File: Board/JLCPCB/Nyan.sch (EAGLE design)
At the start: 63 parts, among them IC1 74HCT541PW, IC2 STM32F10XCXT6, IC3 74HCT541PW, IC4 ST3485, U2 A4988_STEP, U3 MAX6966, X1 WR-WTB2.0-2_THT-VER, X10 32768, X2 WR-WTB2.0-4_THT_VER, X3 WR-WTB2.0-5_THT-VER, X4 WR-WTB2.0-5_THT-VER, X6 68610614122, X7 68612414422, X8 68610414122, X9 8M

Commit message: [Board] A little more layouting done
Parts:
- removed SV1: (no value), con-lstb:MA03-2
- added JP1, JP2: (no value), jumper:JP1E
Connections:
- removed net N$12: R6.2, SV1.2
- removed net N$13: R7.2, SV1.1
- net +3V3: now also JP1.2, JP2.2; no longer SV1.5, SV1.6
- net BOOT1: now also JP2.1, R6.2; no longer SV1.4
- net N$7: now also JP1.1, R7.2; no longer SV1.3
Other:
- moved on the sheet: R6, R7
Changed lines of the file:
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@@
 <part name="SJ1" library="jumper" deviceset="SJ2W" device=""/>
 <part name="SJ2" library="jumper" deviceset="SJ2W" device=""/>
-<part name="SV1" library="con-lstb" deviceset="MA03-2" device=""/>
 <part name="+3V6" library="supply1" deviceset="+3V3" device=""/>
 <part name="R6" library="rcl" deviceset="R-EU_" device="R0603" value="10k"/>
@@
 <part name="C21" library="rcl" deviceset="C-EU" device="C0603" value="1u"/>
 <part name="X3" library="TURAG_Steckverbinder" deviceset="WR-WTB2.0-5" device="_THT-VER"/>
+<part name="JP1" library="jumper" deviceset="JP1E" device=""/>
+<part name="JP2" library="jumper" deviceset="JP1E" device=""/>
 </parts>
 <sheets>
@@
 <instance part="SJ1" gate="G$1" x="40.64" y="30.48" rot="R90"/>
 <instance part="SJ2" gate="G$1" x="40.64" y="12.7" rot="R270"/>
-<instance part="SV1" gate="1" x="27.94" y="-88.9"/>
-<instance part="+3V6" gate="G$1" x="43.18" y="-73.66"/>
-<instance part="R6" gate="G$1" x="17.78" y="-99.06" rot="MR90"/>
-<instance part="R7" gate="G$1" x="38.1" y="-99.06" rot="MR90"/>
+<instance part="+3V6" gate="G$1" x="27.94" y="-73.66"/>
+<instance part="R6" gate="G$1" x="12.7" y="-96.52" rot="MR90"/>
+<instance part="R7" gate="G$1" x="43.18" y="-96.52" rot="MR90"/>
 <instance part="GND15" gate="1" x="58.42" y="-58.42" rot="MR0"/>
 <instance part="GND16" gate="1" x="27.94" y="-111.76" rot="MR0"/>
@@
 <instance part="C21" gate="G$1" x="27.94" y="-43.18" rot="MR180"/>
 <instance part="X3" gate="G$1" x="33.02" y="73.66" rot="R180"/>
+<instance part="JP1" gate="A" x="33.02" y="-88.9" rot="R90"/>
+<instance part="JP2" gate="A" x="22.86" y="-88.9" rot="MR90"/>
 </instances>
 <busses>
@@
 <segment>
 <pinref part="R6" gate="G$1" pin="1"/>
-<wire x1="17.78" y1="-104.14" x2="17.78" y2="-106.68" width="0.1524" layer="91"/>
-<wire x1="17.78" y1="-106.68" x2="27.94" y2="-106.68" width="0.1524" layer="91"/>
+<wire x1="12.7" y1="-101.6" x2="12.7" y2="-106.68" width="0.1524" layer="91"/>
 <pinref part="GND16" gate="1" pin="GND"/>
+<wire x1="12.7" y1="-106.68" x2="27.94" y2="-106.68" width="0.1524" layer="91"/>
 <wire x1="27.94" y1="-106.68" x2="27.94" y2="-109.22" width="0.1524" layer="91"/>
 <pinref part="R7" gate="G$1" pin="1"/>
-<wire x1="27.94" y1="-106.68" x2="38.1" y2="-106.68" width="0.1524" layer="91"/>
-<wire x1="38.1" y1="-106.68" x2="38.1" y2="-104.14" width="0.1524" layer="91"/>
+<wire x1="27.94" y1="-106.68" x2="43.18" y2="-106.68" width="0.1524" layer="91"/>
+<wire x1="43.18" y1="-106.68" x2="43.18" y2="-101.6" width="0.1524" layer="91"/>
 <junction x="27.94" y="-106.68"/>
 </segment>
@@
 </segment>
 <segment>
-<pinref part="SV1" gate="1" pin="5"/>
-<wire x1="35.56" y1="-86.36" x2="43.18" y2="-86.36" width="0.1524" layer="91"/>
-<wire x1="43.18" y1="-86.36" x2="43.18" y2="-78.74" width="0.1524" layer="91"/>
-<pinref part="SV1" gate="1" pin="6"/>
-<wire x1="43.18" y1="-78.74" x2="43.18" y2="-76.2" width="0.1524" layer="91"/>
-<wire x1="20.32" y1="-86.36" x2="17.78" y2="-86.36" width="0.1524" layer="91"/>
-<wire x1="17.78" y1="-86.36" x2="17.78" y2="-78.74" width="0.1524" layer="91"/>
-<wire x1="17.78" y1="-78.74" x2="43.18" y2="-78.74" width="0.1524" layer="91"/>
-<junction x="43.18" y="-78.74"/>
-<pinref part="+3V6" gate="G$1" pin="+3V3"/>
-</segment>
-<segment>
 <pinref part="R8" gate="G$1" pin="2"/>
 <pinref part="+3V7" gate="G$1" pin="+3V3"/>
@@
 <pinref part="+3V1" gate="G$1" pin="+3V3"/>
 </segment>
+<segment>
+<wire x1="35.56" y1="-86.36" x2="38.1" y2="-86.36" width="0.1524" layer="91"/>
+<wire x1="38.1" y1="-86.36" x2="38.1" y2="-78.74" width="0.1524" layer="91"/>
+<wire x1="20.32" y1="-86.36" x2="17.78" y2="-86.36" width="0.1524" layer="91"/>
+<wire x1="17.78" y1="-86.36" x2="17.78" y2="-78.74" width="0.1524" layer="91"/>
+<wire x1="17.78" y1="-78.74" x2="27.94" y2="-78.74" width="0.1524" layer="91"/>
+<pinref part="JP1" gate="A" pin="2"/>
+<pinref part="JP2" gate="A" pin="2"/>
+<pinref part="+3V6" gate="G$1" pin="+3V3"/>
+<wire x1="27.94" y1="-78.74" x2="38.1" y2="-78.74" width="0.1524" layer="91"/>
+<wire x1="27.94" y1="-76.2" x2="27.94" y2="-78.74" width="0.1524" layer="91"/>
+<junction x="27.94" y="-78.74"/>
+</segment>
 </net>
 <net name="M2B" class="0">
@@
 </segment>
 <segment>
-<pinref part="SV1" gate="1" pin="4"/>
-<wire x1="20.32" y1="-88.9" x2="5.08" y2="-88.9" width="0.1524" layer="91"/>
+<wire x1="20.32" y1="-88.9" x2="12.7" y2="-88.9" width="0.1524" layer="91"/>
 <label x="5.08" y="-88.9" size="1.778" layer="95"/>
+<pinref part="R6" gate="G$1" pin="2"/>
+<wire x1="12.7" y1="-88.9" x2="5.08" y2="-88.9" width="0.1524" layer="91"/>
+<wire x1="12.7" y1="-91.44" x2="12.7" y2="-88.9" width="0.1524" layer="91"/>
+<junction x="12.7" y="-88.9"/>
+<pinref part="JP2" gate="A" pin="1"/>
 </segment>
 </net>
 <net name="N$7" class="0">
 <segment>
-<pinref part="SV1" gate="1" pin="3"/>
 <pinref part="IC2" gate="RESET" pin="BOOT0"/>
-<wire x1="35.56" y1="-88.9" x2="60.96" y2="-88.9" width="0.1524" layer="91"/>
-</segment>
-</net>
-<net name="N$12" class="0">
-<segment>
-<pinref part="R6" gate="G$1" pin="2"/>
-<pinref part="SV1" gate="1" pin="2"/>
-<wire x1="17.78" y1="-93.98" x2="17.78" y2="-91.44" width="0.1524" layer="91"/>
-<wire x1="17.78" y1="-91.44" x2="20.32" y2="-91.44" width="0.1524" layer="91"/>
-</segment>
-</net>
-<net name="N$13" class="0">
-<segment>
-<pinref part="SV1" gate="1" pin="1"/>
+<wire x1="35.56" y1="-88.9" x2="43.18" y2="-88.9" width="0.1524" layer="91"/>
 <pinref part="R7" gate="G$1" pin="2"/>
-<wire x1="35.56" y1="-91.44" x2="38.1" y2="-91.44" width="0.1524" layer="91"/>
-<wire x1="38.1" y1="-91.44" x2="38.1" y2="-93.98" width="0.1524" layer="91"/>
-</segment>
-</net>
+<wire x1="43.18" y1="-88.9" x2="60.96" y2="-88.9" width="0.1524" layer="91"/>
+<wire x1="43.18" y1="-91.44" x2="43.18" y2="-88.9" width="0.1524" layer="91"/>
+<junction x="43.18" y="-88.9"/>
+<pinref part="JP1" gate="A" pin="1"/>
+</segment>
+</net>

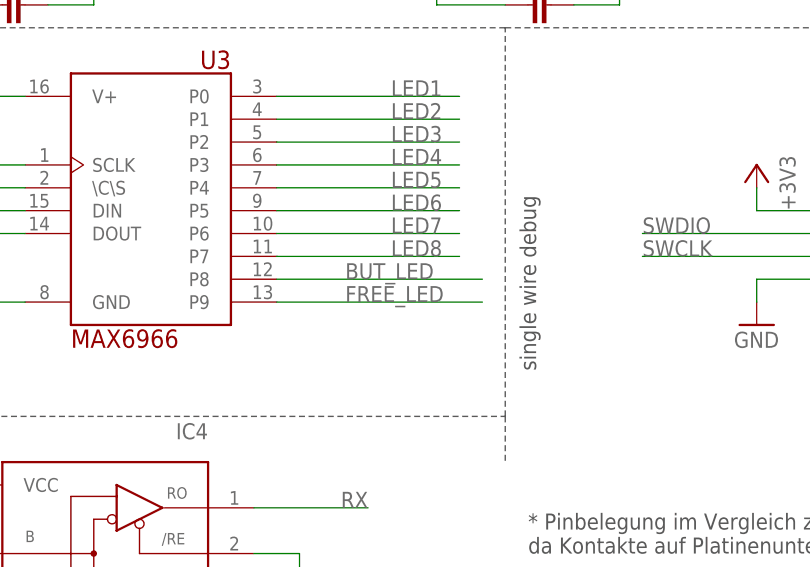
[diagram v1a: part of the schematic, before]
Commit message: [Board] Some progress in routing
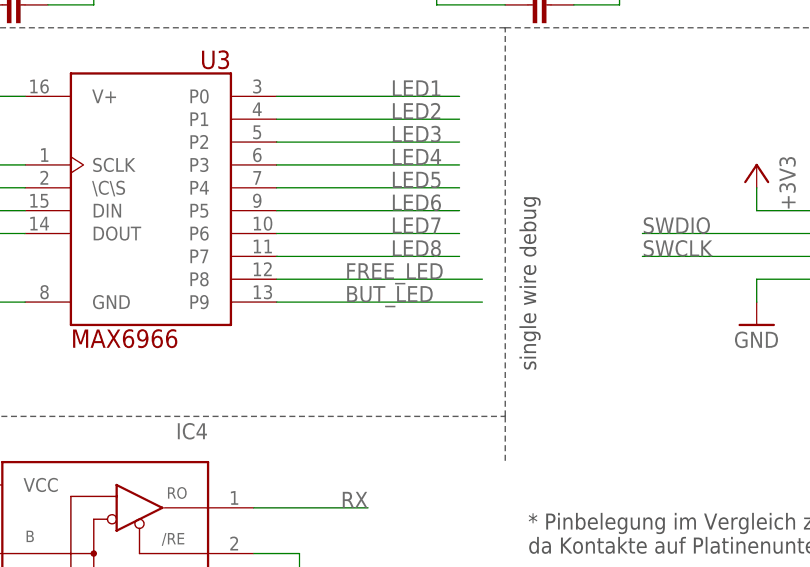
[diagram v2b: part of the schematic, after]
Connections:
- net BUT_LED: now also U3.P9; no longer U3.P8
- net FREE_LED: now also U3.P8; no longer U3.P9
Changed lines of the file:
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@@
 </segment>
 <segment>
-<pinref part="U3" gate="G$1" pin="P8"/>
-<wire x1="137.16" y1="55.88" x2="160.02" y2="55.88" width="0.1524" layer="91"/>
-<label x="144.78" y="55.88" size="1.778" layer="95"/>
+<pinref part="U3" gate="G$1" pin="P9"/>
+<wire x1="137.16" y1="53.34" x2="160.02" y2="53.34" width="0.1524" layer="91"/>
+<label x="144.78" y="53.34" size="1.778" layer="95"/>
 </segment>
 </net>
@@
 <net name="FREE_LED" class="0">
 <segment>
-<pinref part="U3" gate="G$1" pin="P9"/>
-<wire x1="137.16" y1="53.34" x2="160.02" y2="53.34" width="0.1524" layer="91"/>
-<label x="144.78" y="53.34" size="1.778" layer="95"/>
-</segment>
-<segment>
 <wire x1="35.56" y1="50.8" x2="48.26" y2="50.8" width="0.1524" layer="91"/>
 <label x="43.18" y="50.8" size="1.778" layer="95"/>
 <pinref part="X4" gate="G$1" pin="2"/>
 </segment>
-</net>
+<segment>
+<pinref part="U3" gate="G$1" pin="P8"/>
+<wire x1="137.16" y1="55.88" x2="160.02" y2="55.88" width="0.1524" layer="91"/>
+<label x="144.78" y="55.88" size="1.778" layer="95"/>
+</segment>
+</net>

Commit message: [Board] More layouting done
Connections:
- net N$7 renamed BOOT0
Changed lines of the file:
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@@
 </segment>
 </net>
-<net name="N$7" class="0">
+<net name="BOOT0" class="0">
 <segment>
 <pinref part="IC2" gate="RESET" pin="BOOT0"/>
@@
 <junction x="43.18" y="-88.9"/>
 <pinref part="JP1" gate="A" pin="1"/>
+<label x="43.18" y="-88.9" size="1.778" layer="95"/>
 </segment>
 </net>

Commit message: [Board] More layouting
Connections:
- net +3V3: now also R1.2, R2.2, R4.2
- net +5V: no longer R1.2, R2.2, R4.2
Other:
- moved on the sheet: R4
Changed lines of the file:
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@@
 <part name="GND9" library="supply1" deviceset="GND" device=""/>
 <part name="R1" library="rcl" deviceset="R-EU_" device="R0603" value="300"/>
-<part name="P+8" library="supply1" deviceset="+5V" device=""/>
 <part name="P+9" library="supply1" deviceset="+5V" device=""/>
 <part name="P+10" library="supply1" deviceset="+12V" device=""/>
@@
 <part name="JP1" library="jumper" deviceset="JP1E" device=""/>
 <part name="JP2" library="jumper" deviceset="JP1E" device=""/>
+<part name="+3V12" library="supply1" deviceset="+3V3" device=""/>
+<part name="+3V13" library="supply1" deviceset="+3V3" device=""/>
 </parts>
 <sheets>
@@
 <instance part="GND9" gate="1" x="25.4" y="12.7"/>
 <instance part="R1" gate="G$1" x="238.76" y="55.88" rot="R90"/>
-<instance part="P+8" gate="1" x="248.92" y="71.12"/>
 <instance part="P+9" gate="1" x="228.6" y="116.84"/>
 <instance part="P+10" gate="1" x="228.6" y="144.78"/>
@@
 <instance part="+3V4" gate="G$1" x="228.6" y="177.8"/>
 <instance part="R3" gate="G$1" x="228.6" y="167.64" rot="R90"/>
-<instance part="R4" gate="G$1" x="220.98" y="104.14"/>
+<instance part="R4" gate="G$1" x="213.36" y="119.38" rot="R90"/>
 <instance part="+3V5" gate="G$1" x="78.74" y="38.1" rot="MR0"/>
 <instance part="GND13" gate="1" x="78.74" y="7.62" rot="MR0"/>
@@
 <instance part="JP1" gate="A" x="33.02" y="-88.9" rot="R90"/>
 <instance part="JP2" gate="A" x="22.86" y="-88.9" rot="MR90"/>
+<instance part="+3V12" gate="G$1" x="248.92" y="71.12" rot="MR0"/>
+<instance part="+3V13" gate="G$1" x="213.36" y="132.08"/>
 </instances>
 <busses>
@@
 </segment>
 <segment>
-<pinref part="P+8" gate="1" pin="+5V"/>
-<pinref part="R1" gate="G$1" pin="2"/>
-<wire x1="248.92" y1="68.58" x2="248.92" y2="63.5" width="0.1524" layer="91"/>
-<pinref part="R2" gate="G$1" pin="2"/>
-<wire x1="248.92" y1="63.5" x2="238.76" y2="63.5" width="0.1524" layer="91"/>
-<wire x1="238.76" y1="63.5" x2="238.76" y2="60.96" width="0.1524" layer="91"/>
-<wire x1="248.92" y1="63.5" x2="248.92" y2="60.96" width="0.1524" layer="91"/>
-<junction x="248.92" y="63.5"/>
-</segment>
-<segment>
 <pinref part="X7" gate="G$1" pin="14"/>
 <wire x1="251.46" y1="104.14" x2="228.6" y2="104.14" width="0.1524" layer="91"/>
@@
 <pinref part="P+9" gate="1" pin="+5V"/>
 <wire x1="228.6" y1="104.14" x2="228.6" y2="114.3" width="0.1524" layer="91"/>
-<pinref part="R4" gate="G$1" pin="2"/>
-<wire x1="226.06" y1="104.14" x2="228.6" y2="104.14" width="0.1524" layer="91"/>
-<junction x="228.6" y="104.14"/>
 </segment>
 <segment>
@@
 <junction x="27.94" y="-78.74"/>
 </segment>
+<segment>
+<pinref part="R1" gate="G$1" pin="2"/>
+<wire x1="248.92" y1="68.58" x2="248.92" y2="63.5" width="0.1524" layer="91"/>
+<pinref part="R2" gate="G$1" pin="2"/>
+<wire x1="248.92" y1="63.5" x2="238.76" y2="63.5" width="0.1524" layer="91"/>
+<wire x1="238.76" y1="63.5" x2="238.76" y2="60.96" width="0.1524" layer="91"/>
+<wire x1="248.92" y1="63.5" x2="248.92" y2="60.96" width="0.1524" layer="91"/>
+<junction x="248.92" y="63.5"/>
+<pinref part="+3V12" gate="G$1" pin="+3V3"/>
+</segment>
+<segment>
+<pinref part="R4" gate="G$1" pin="2"/>
+<pinref part="+3V13" gate="G$1" pin="+3V3"/>
+<wire x1="213.36" y1="129.54" x2="213.36" y2="124.46" width="0.1524" layer="91"/>
+</segment>
 </net>
 <net name="M2B" class="0">
@@
 <pinref part="X7" gate="G$1" pin="12"/>
 <wire x1="251.46" y1="109.22" x2="213.36" y2="109.22" width="0.1524" layer="91"/>
-<wire x1="213.36" y1="109.22" x2="213.36" y2="104.14" width="0.1524" layer="91"/>
 <pinref part="R4" gate="G$1" pin="1"/>
-<wire x1="213.36" y1="104.14" x2="215.9" y2="104.14" width="0.1524" layer="91"/>
+<wire x1="213.36" y1="109.22" x2="213.36" y2="114.3" width="0.1524" layer="91"/>
 <wire x1="213.36" y1="109.22" x2="205.74" y2="109.22" width="0.1524" layer="91"/>
 <junction x="213.36" y="109.22"/>
